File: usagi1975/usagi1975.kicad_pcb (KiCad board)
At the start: 2 copper layers, 15 parts

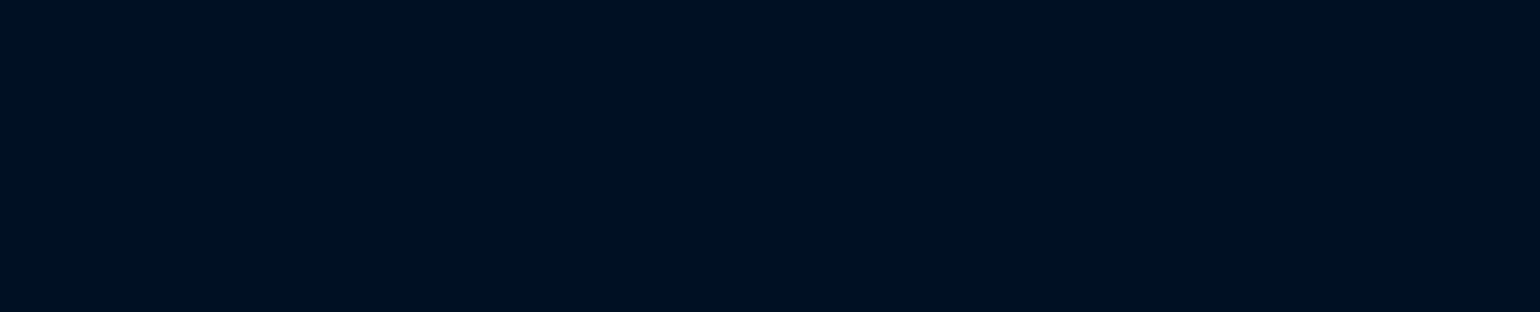
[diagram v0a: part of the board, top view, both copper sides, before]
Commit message: modified illustrator files
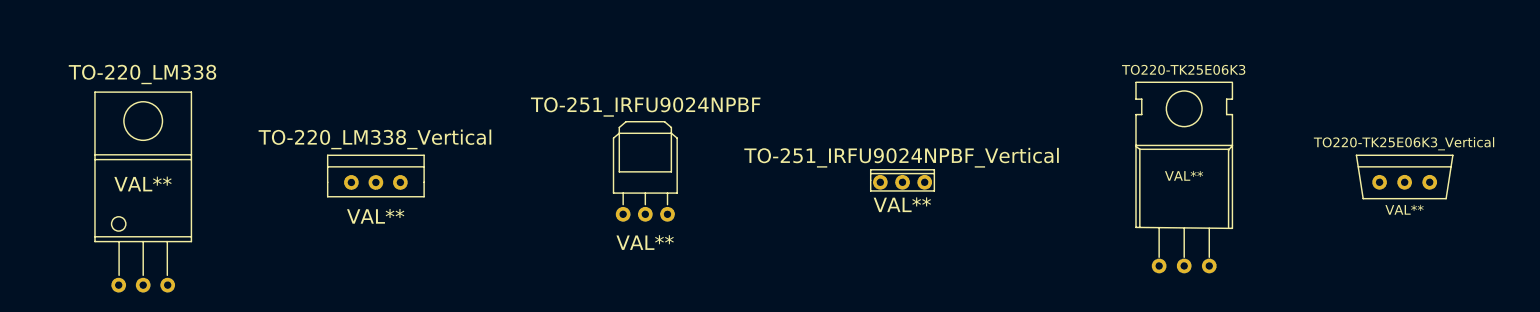
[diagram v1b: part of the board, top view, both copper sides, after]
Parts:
- added TO-220_LM338: VAL**, kicad_mod:TO-220_LM338, F.Cu at (36.8, 109.2)
- added TO-220_LM338_Vertical: VAL**, kicad_mod:TO-220_LM338_Vertical, F.Cu at (61.0, 115.6)
- added TO-251_IRFU9024NPBF: VAL**, kicad_mod:TO-251_IRFU9024NPBF, F.Cu at (88.9, 110.5)
- added TO-251_IRFU9024NPBF_Vertical: VAL**, kicad_mod:TO-251_IRFU9024NPBF_Vertical, F.Cu at (115.6, 115.6)
- added TO220-TK25E06K3: VAL**, kicad_mod:TO220-TK25E06K3, F.Cu at (144.8, 108.0)
- added TO220-TK25E06K3_Vertical: VAL**, kicad_mod:TO220-TK25E06K3_Vertical, F.Cu at (167.6, 115.6)
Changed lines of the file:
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@@
     (tracks 0)
     (zones 0)
-    (modules 15)
+    (modules 21)
     (nets 1)
   )
@@
     )
   )
+  (module kicad_mod:TO-220_LM338 (layer F.Cu)
+    (at 36.83 109.22)
+    (fp_text reference TO-220_LM338 (at 0 -5) (layer F.SilkS)
+      (effects (font (size 1.5 1.5) (thickness 0.15)))
+    )
+    (fp_text value VAL** (at 0 6.6) (layer F.SilkS)
+      (effects (font (size 1.5 1.5) (thickness 0.15)))
+    )
+    (fp_circle (center -2.54 10.668) (end -1.905 11.049) (layer F.SilkS) (width 0.15))
+    (fp_line (start 2.5 12.5) (end 2.5 16) (layer F.SilkS) (width 0.15))
+    (fp_line (start 0 12.5) (end 0 16) (layer F.SilkS) (width 0.15))
+    (fp_line (start -2.5 12.5) (end -2.5 16) (layer F.SilkS) (width 0.15))
+    (fp_line (start -5 12) (end 5 12) (layer F.SilkS) (width 0.15))
+    (fp_line (start -5 4) (end 5 4) (layer F.SilkS) (width 0.15))
+    (fp_line (start 5 3.5) (end 5 12.5) (layer F.SilkS) (width 0.15))
+    (fp_line (start 5 12.5) (end -5 12.5) (layer F.SilkS) (width 0.15))
+    (fp_line (start -5 12.5) (end -5 3.5) (layer F.SilkS) (width 0.15))
+    (fp_line (start -5 -3) (end -5 3.5) (layer F.SilkS) (width 0.15))
+    (fp_line (start -5 3.5) (end 5 3.5) (layer F.SilkS) (width 0.15))
+    (fp_line (start 5 -3) (end 5 3.5) (layer F.SilkS) (width 0.15))
+    (fp_line (start -5 -3) (end 5 -3) (layer F.SilkS) (width 0.15))
+    (fp_circle (center 0 0) (end 2 0) (layer F.SilkS) (width 0.15))
+    (pad 2 thru_hole circle (at 0 17.018) (size 1.524 1.524) (drill 0.762) (layers *.Cu *.Mask F.SilkS))
+    (pad 1 thru_hole circle (at -2.54 17.018) (size 1.524 1.524) (drill 0.762) (layers *.Cu *.Mask F.SilkS))
+    (pad 3 thru_hole circle (at 2.54 17.018) (size 1.524 1.524) (drill 0.762) (layers *.Cu *.Mask F.SilkS))
+  )
+  (module kicad_mod:TO-220_LM338_Vertical (layer F.Cu)
+    (at 60.96 115.57)
+    (fp_text reference TO-220_LM338_Vertical (at 0 -4.6) (layer F.SilkS)
+      (effects (font (size 1.5 1.5) (thickness 0.15)))
+    )
+    (fp_text value VAL** (at 0 3.6) (layer F.SilkS)
+      (effects (font (size 1.5 1.5) (thickness 0.15)))
+    )
+    (fp_line (start 5 -1.6) (end -5 -1.6) (layer F.SilkS) (width 0.15))
+    (fp_line (start 5 0) (end 5 -2.8) (layer F.SilkS) (width 0.15))
+    (fp_line (start 5 -2.8) (end -5 -2.8) (layer F.SilkS) (width 0.15))
+    (fp_line (start -5 -2.8) (end -5 0) (layer F.SilkS) (width 0.15))
+    (fp_line (start -5 0) (end -5 1.5) (layer F.SilkS) (width 0.15))
+    (fp_line (start -5 1.5) (end 5 1.5) (layer F.SilkS) (width 0.15))
+    (fp_line (start 5 1.5) (end 5 0) (layer F.SilkS) (width 0.15))
+    (pad 2 thru_hole circle (at 0 0.018) (size 1.524 1.524) (drill 0.762) (layers *.Cu *.Mask F.SilkS))
+    (pad 1 thru_hole circle (at -2.54 0.018) (size 1.524 1.524) (drill 0.762) (layers *.Cu *.Mask F.SilkS))
+    (pad 3 thru_hole circle (at 2.54 0.018) (size 1.524 1.524) (drill 0.762) (layers *.Cu *.Mask F.SilkS))
+  )
+  (module kicad_mod:TO-251_IRFU9024NPBF (layer F.Cu)
+    (at 88.9 110.49)
+    (fp_text reference TO-251_IRFU9024NPBF (at 0.1 -2.9) (layer F.SilkS)
+      (effects (font (size 1.5 1.5) (thickness 0.15)))
+    )
+    (fp_text value VAL** (at 0 11.4) (layer F.SilkS)
+      (effects (font (size 1.5 1.5) (thickness 0.15)))
+    )
+    (fp_line (start -2.7 0) (end -2.7 4) (layer F.SilkS) (width 0.15))
+    (fp_line (start -2.7 4) (end 2.7 4) (layer F.SilkS) (width 0.15))
+    (fp_line (start 2.7 4) (end 2.7 0) (layer F.SilkS) (width 0.15))
+    (fp_line (start 2.3 6.2) (end 2.3 7.4) (layer F.SilkS) (width 0.15))
+    (fp_line (start -2.3 6.2) (end -2.3 7.4) (layer F.SilkS) (width 0.15))
+    (fp_line (start 0 7.4) (end 0 6.2) (layer F.SilkS) (width 0.15))
+    (fp_line (start 3.3 0.5) (end 3.3 6.2) (layer F.SilkS) (width 0.15))
+    (fp_line (start -3.3 0.5) (end -3.3 6.2) (layer F.SilkS) (width 0.15))
+    (fp_line (start 2.7 0) (end 3.3 0.5) (layer F.SilkS) (width 0.15))
+    (fp_line (start -2.7 0) (end -3.3 0.5) (layer F.SilkS) (width 0.15))
+    (fp_line (start 3.3 6.2) (end -3.3 6.2) (layer F.SilkS) (width 0.15))
+    (fp_line (start -2.7 -0.6) (end -2.7 0) (layer F.SilkS) (width 0.15))
+    (fp_line (start 2 -1.2) (end -2 -1.2) (layer F.SilkS) (width 0.15))
+    (fp_line (start 2.7 0) (end 2.7 -0.6) (layer F.SilkS) (width 0.15))
+    (fp_line (start 2.7 -0.6) (end 2 -1.2) (layer F.SilkS) (width 0.15))
+    (fp_line (start -2.7 -0.6) (end -2 -1.2) (layer F.SilkS) (width 0.15))
+    (fp_line (start 2.7 0) (end -2.7 0) (layer F.SilkS) (width 0.15))
+    (pad 2 thru_hole circle (at 0 8.4) (size 1.524 1.524) (drill 0.762) (layers *.Cu *.Mask F.SilkS))
+    (pad 1 thru_hole circle (at -2.3 8.4) (size 1.524 1.524) (drill 0.762) (layers *.Cu *.Mask F.SilkS))
+    (pad 3 thru_hole circle (at 2.3 8.4) (size 1.524 1.524) (drill 0.762) (layers *.Cu *.Mask F.SilkS))
+  )
+  (module kicad_mod:TO-251_IRFU9024NPBF_Vertical (layer F.Cu)
+    (at 115.57 115.57)
+    (fp_text reference TO-251_IRFU9024NPBF_Vertical (at 0 -2.7) (layer F.SilkS)
+      (effects (font (size 1.5 1.5) (thickness 0.15)))
+    )
+    (fp_text value VAL** (at 0 2.4) (layer F.SilkS)
+      (effects (font (size 1.5 1.5) (thickness 0.15)))
+    )
+    (fp_line (start -3.3 -0.9) (end 3.3 -0.9) (layer F.SilkS) (width 0.15))
+    (fp_line (start -3.3 -0.2) (end -3.3 -1.3) (layer F.SilkS) (width 0.15))
+    (fp_line (start -3.3 -1.3) (end 3.3 -1.3) (layer F.SilkS) (width 0.15))
+    (fp_line (start 3.3 -1.3) (end 3.3 0.9) (layer F.SilkS) (width 0.15))
+    (fp_line (start 3.3 0.9) (end -3.3 0.9) (layer F.SilkS) (width 0.15))
+    (fp_line (start -3.3 0.9) (end -3.3 -0.2) (layer F.SilkS) (width 0.15))
+    (pad 2 thru_hole circle (at 0 0) (size 1.524 1.524) (drill 0.762) (layers *.Cu *.Mask F.SilkS))
+    (pad 1 thru_hole circle (at -2.3 0) (size 1.524 1.524) (drill 0.762) (layers *.Cu *.Mask F.SilkS))
+    (pad 3 thru_hole circle (at 2.3 0) (size 1.524 1.524) (drill 0.762) (layers *.Cu *.Mask F.SilkS))
+  )
+  (module kicad_mod:TO220-TK25E06K3 (layer F.Cu)
+    (at 144.78 107.95)
+    (fp_text reference TO220-TK25E06K3 (at 0 -4) (layer F.SilkS)
+      (effects (font (size 1 1) (thickness 0.15)))
+    )
+    (fp_text value VAL** (at 0 7) (layer F.SilkS)
+      (effects (font (size 1 1) (thickness 0.15)))
+    )
+    (fp_line (start -5 3.8) (end -5 0.6) (layer F.SilkS) (width 0.15))
+    (fp_line (start -5 -1) (end -5 -2.7) (layer F.SilkS) (width 0.15))
+    (fp_line (start 5 0.6) (end 5 3.8) (layer F.SilkS) (width 0.15))
+    (fp_line (start 5 -2.7) (end 5 -1) (layer F.SilkS) (width 0.15))
+    (fp_line (start -5 0.6) (end -4.4 0.6) (layer F.SilkS) (width 0.15))
+    (fp_line (start -4.4 0.6) (end -4.4 -1) (layer F.SilkS) (width 0.15))
+    (fp_line (start -4.4 -1) (end -5 -1) (layer F.SilkS) (width 0.15))
+    (fp_line (start 5 0.6) (end 4.4 0.6) (layer F.SilkS) (width 0.15))
+    (fp_line (start 4.4 0.6) (end 4.4 -1) (layer F.SilkS) (width 0.15))
+    (fp_line (start 4.4 -1) (end 5 -1) (layer F.SilkS) (width 0.15))
+    (fp_line (start 5 3.8) (end 4.6 4.3) (layer F.SilkS) (width 0.15))
+    (fp_line (start -5 3.9) (end -4.6 4.2) (layer F.SilkS) (width 0.15))
+    (fp_line (start -4.6 12.3) (end -4.6 4.2) (layer F.SilkS) (width 0.15))
+    (fp_line (start -4.6 4.2) (end 4.6 4.2) (layer F.SilkS) (width 0.15))
+    (fp_line (start 4.6 4.2) (end 4.6 12.3) (layer F.SilkS) (width 0.15))
+    (fp_line (start 2.6 15.4) (end 2.6 12.4) (layer F.SilkS) (width 0.15))
+    (fp_line (start -2.6 15.4) (end -2.6 12.4) (layer F.SilkS) (width 0.15))
+    (fp_line (start 0 12.4) (end 0 15.4) (layer F.SilkS) (width 0.15))
+    (fp_line (start 5 3.8) (end 5 12.4) (layer F.SilkS) (width 0.15))
+    (fp_line (start 5 12.4) (end -5 12.3) (layer F.SilkS) (width 0.15))
+    (fp_line (start -5 12.3) (end -5 3.8) (layer F.SilkS) (width 0.15))
+    (fp_line (start 5 3.8) (end -5 3.8) (layer F.SilkS) (width 0.15))
+    (fp_line (start -5 -2.75) (end 5 -2.75) (layer F.SilkS) (width 0.15))
+    (fp_circle (center 0 0) (end 1.85 0) (layer F.SilkS) (width 0.15))
+    (pad 2 thru_hole circle (at 0 16.3) (size 1.524 1.524) (drill 0.762) (layers *.Cu *.Mask F.SilkS))
+    (pad 1 thru_hole circle (at -2.6 16.3) (size 1.524 1.524) (drill 0.762) (layers *.Cu *.Mask F.SilkS))
+    (pad 3 thru_hole circle (at 2.6 16.3) (size 1.524 1.524) (drill 0.762) (layers *.Cu *.Mask F.SilkS))
+  )
+  (module kicad_mod:TO220-TK25E06K3_Vertical (layer F.Cu)
+    (at 167.64 115.57)
+    (fp_text reference TO220-TK25E06K3_Vertical (at 0 -4.1) (layer F.SilkS)
+      (effects (font (size 1 1) (thickness 0.15)))
+    )
+    (fp_text value VAL** (at 0 2.9) (layer F.SilkS)
+      (effects (font (size 1 1) (thickness 0.15)))
+    )
+    (fp_line (start 4.8 -1.6) (end -4.8 -1.6) (layer F.SilkS) (width 0.15))
+    (fp_line (start -4.3 1.7) (end 4.3 1.7) (layer F.SilkS) (width 0.15))
+    (fp_line (start 5 -2.8) (end 4.3 1.7) (layer F.SilkS) (width 0.15))
+    (fp_line (start -5 -2.8) (end -4.3 1.7) (layer F.SilkS) (width 0.15))
+    (fp_line (start 5 -2.8) (end -5 -2.8) (layer F.SilkS) (width 0.15))
+    (pad 2 thru_hole circle (at 0 0) (size 1.524 1.524) (drill 0.762) (layers *.Cu *.Mask F.SilkS))
+    (pad 1 thru_hole circle (at -2.6 0) (size 1.524 1.524) (drill 0.762) (layers *.Cu *.Mask F.SilkS))
+    (pad 3 thru_hole circle (at 2.6 0) (size 1.524 1.524) (drill 0.762) (layers *.Cu *.Mask F.SilkS))
+  )
 )
